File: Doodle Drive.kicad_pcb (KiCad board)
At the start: 2 copper layers, 62.9 x 80 mm, 101 parts, among them J1 USB_B, J12 PINHD_1x4_Male, J15 PINHD_1x4_Male, J2 PINHD_1x4_Male, J3 Screw_Terminal_01x02, J6 PINHD_1x2_Male, J8 PINHD_1x4_Male, J9 PINHD_1x4_Male, SW1 Push_Button, SW2 Push_Button, SW3 Push_Button, U1 STM32F411RETx, U2 DRV8825PWP, U3 DRV8825PWP, U4 DRV8825PWP, U5 DRV8825PWP, U6 AP7343-30W5-7, U7 CP2102-GMR_NRND, Y1 32.768KHz ±20ppm 12.5pF, Y2 25MHZ 9PF

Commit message: deTommaso approved version
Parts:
- removed RV5: R_Potentiometer, poti:3386P1473LF
- removed TP1, TP2, TP42, TP5: TestPoint, TestPoint:TestPoint_Pad_D1.5mm
- added RV4: R_Potentiometer, poti:3386P1473LF, F.Cu at (84.8, 73.1)
- C18, C22, C27, C32: value Bulk Capacitance. 4.7uF? -> 10uF; footprint Capacitor_SMD:C_0805_2012Metric -> Capacitor_THT:C_Radial_D5.0mm_H5.0mm_P2.00mm
- moved C11 205.5 mm to (137.2, 111.8), turned to -90 degrees
- moved C5 205.3 mm to (135.9, 114.3), turned to 180 degrees
- moved R14 202.7 mm to (135.3, 111.1), turned to 90 degrees
- moved R12 202.0 mm to (136.0, 108.0), turned to 0 degrees
- moved R13 201.1 mm to (136.0, 106.0), turned to 180 degrees
- moved R5 200.1 mm to (136.0, 104.1), turned to 0 degrees
- moved J8 199.6 mm to (131.4, 114.3), turned to -90 degrees
- moved C20 197.7 mm to (136.3, 97.8), turned to 0 degrees
- moved C21 196.7 mm to (136.3, 95.2), turned to 0 degrees
- moved U2 192.1 mm to (128.8, 107.1), turned to 180 degrees
- moved RV1 189.6 mm to (130.9, 95.9), turned to 0 degrees
- moved C18 186.8 mm to (137.2, 86.4), turned to 180 degrees
- moved R18 186.4 mm to (122.7, 111.1), turned to 0 degrees
- moved R19 183.3 mm to (123.0, 104.8), turned to 0 degrees
- moved C16 180.3 mm to (117.6, 111.8), turned to -90 degrees
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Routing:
- net GND: track 407.9 -> 518.0 mm, vias 8 -> 14
- net +3V3: track 221.9 -> 241.3 mm
- net +15V: track 304.9 -> 320.9 mm
- net Net-(U2-AVREF): track 20.7 -> 14.3 mm
- net Net-(U5-AVREF): track 21.0 -> 14.6 mm
- net Net-(U3-AVREF): track 21.5 -> 15.1 mm
- net Net-(U4-AVREF): track 20.7 -> 14.4 mm
- net PA14: track 20.7 -> 25.5 mm
- net PA13: track 9.06 -> 13.4 mm
- net PB13: track 40.1 -> 43.0 mm
- net PB6: track 30.3 -> 28.2 mm
- net PB14: track 32.2 -> 34.2 mm
- net PB15: track 29.9 -> 31.6 mm
- net +5V: track 65.5 -> 67.1 mm
- net PB12: track 43.4 -> 44.8 mm
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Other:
- board size 62.9 x 80 mm -> 80 x 62.9 mm

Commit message: bestellte version
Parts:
- C10, C7: footprint Capacitor_SMD:C_0805_2012Metric -> Capacitor_SMD:C_0402_1005Metric
- C11, C16, C26, C31: value 100nF 16V ceramic -> 100nF
- C15, C25, C30, C5: value 10nF 50V -> 10nF
- C20, C21, C23, C24, C28, C29, C33, C34: value 100nF 50V -> 100nF
- C6, C9: value 12pF -> 18pF
- L1: value 10uH ±10% -> 10uH
- R12, R13, R15, R16, R24, R25, R33, R34: footprint Resistor_SMD:R_0805_2012Metric -> Resistor_SMD:R_1206_3216Metric
- R4: value 0 -> 0ohm
- U6: value AP7343-30W5-7 -> AP7343-33W5-7
- U7: value CP2102-GMR_NRND -> CP2102-GMR
- Y2: value 25MHZ 9PF -> 25MHZ 12PF
- moved R39 77.9 mm to (136.8, 130.9), turned to 90 degrees
- moved R40 73.8 mm to (130.5, 130.9), turned to 90 degrees
- moved D6 73.8 mm to (127.3, 132.2), turned to 0 degrees
- moved J15 69.3 mm to (140.0, 121.6), turned to 0 degrees
- moved U5 67.5 mm to (132.7, 124.8), turned to -90 degrees
- moved C30 65.0 mm to (140.6, 117.0), turned to -90 degrees
- moved J3 62.4 mm to (104.2, 126.9), turned to 0 degrees
- moved R35 62.2 mm to (136.8, 117.6), turned to 180 degrees
- moved C31 60.7 mm to (137.5, 115.7), turned to 0 degrees
- moved R33 59.3 mm to (133.5, 117.0), turned to 90 degrees
- moved RV3 58.5 mm to (121.6, 122.7), turned to 90 degrees
- moved J1 57.8 mm to (95.4, 121.5), turned to 180 degrees
- moved C5 57.7 mm to (140.6, 56.8), turned to -90 degrees
- moved R34 57.1 mm to (131.0, 117.0), turned to -90 degrees
- moved C11 56.3 mm to (138.1, 55.5), turned to 0 degrees
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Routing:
- net GND: track 518.0 -> 541.4 mm, vias 14 -> 15
- net +3V3: track 241.3 -> 235.8 mm
- net +15V: track 320.9 -> 325.6 mm
- net PC14: track 10.9 -> 8.61 mm
- net PC15: track 8.78 -> 7.83 mm
- net Net-(U3-AVREF): track 15.1 -> 14.9 mm, vias 2 -> 1
- net Net-(U5-AVREF): track 14.6 -> 14.8 mm, vias 2 -> 1
- net Net-(U4-AVREF): vias 2 -> 1
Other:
- board size 80 x 62.9 mm -> 62.9 x 80 mm
- board text added: "5BEL 12/2023"
- board text added: "Doodle Drive V1.0"
- board text added: "ELIA VANDINI"

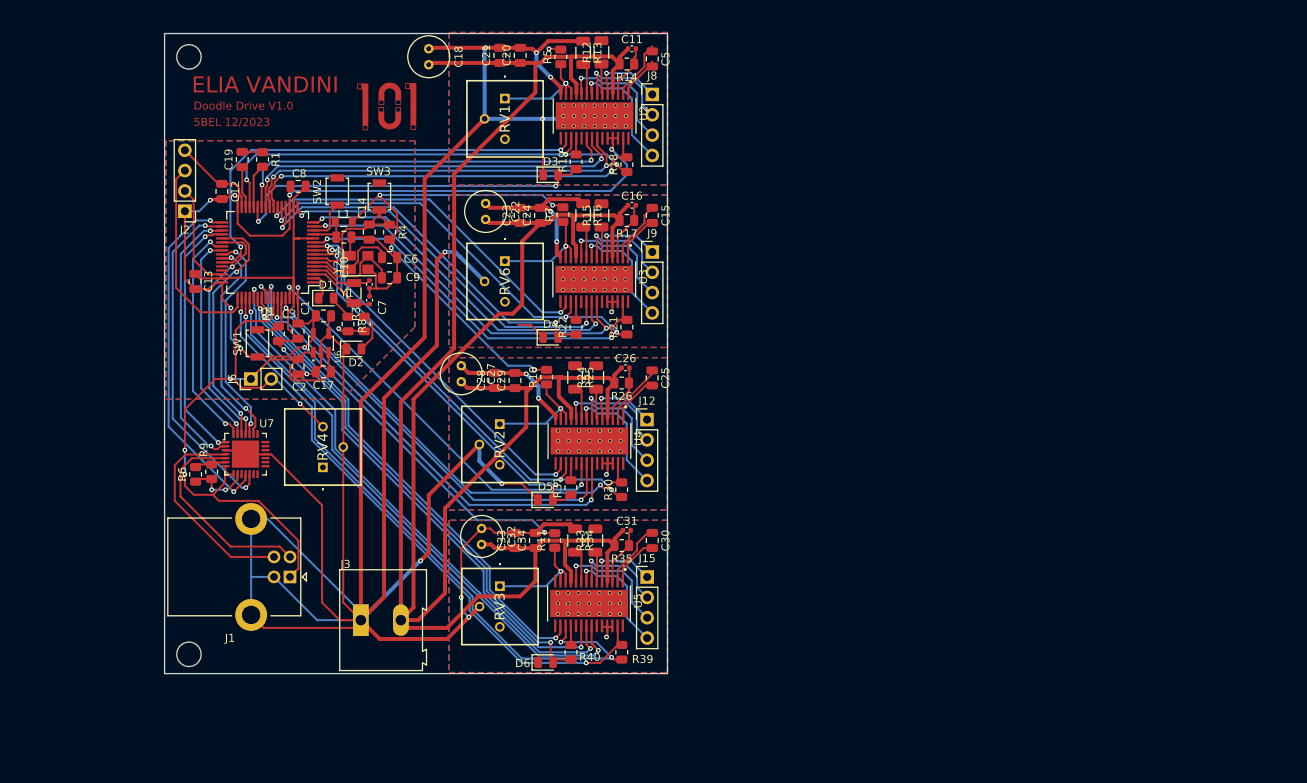
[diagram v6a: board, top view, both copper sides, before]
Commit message: reworked single motor drive module
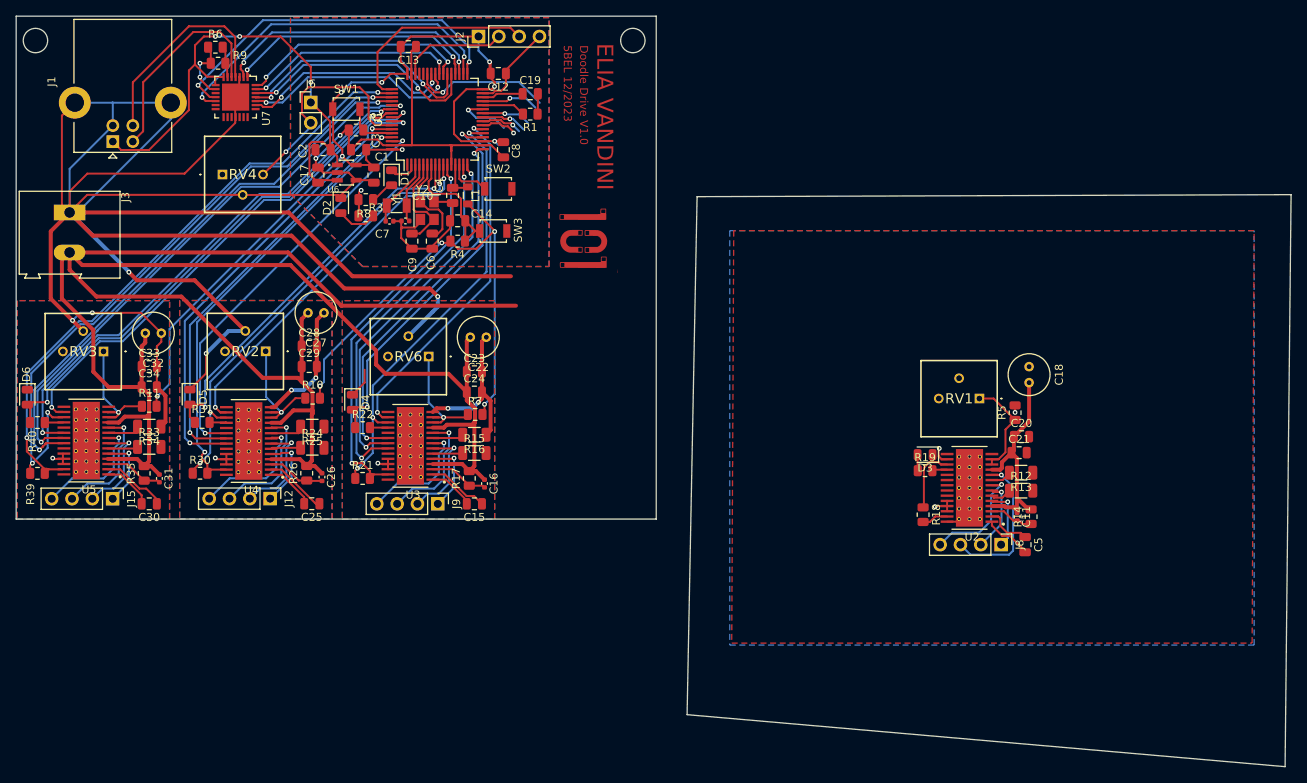
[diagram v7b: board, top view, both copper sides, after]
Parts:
- moved C18 84.9 mm to (187.8, 95.2)
- moved C21 81.7 mm to (186.5, 106.0), turned to 0 degrees
- moved C20 78.7 mm to (186.8, 104.0), turned to 0 degrees
- moved C5 76.5 mm to (187.2, 117.5)
- moved R39 76.4 mm to (63.8, 108.6), turned to 0 degrees
- moved R14 75.9 mm to (188.0, 114.0), turned to 90 degrees
- moved R12 75.9 mm to (186.8, 110.8), turned to 0 degrees
- moved R13 75.8 mm to (186.8, 108.5), turned to 180 degrees
- moved C11 75.8 mm to (186.2, 114.0), turned to -90 degrees
- moved D6 72.8 mm to (62.5, 99.1), turned to -90 degrees
- moved R40 72.6 mm to (63.8, 102.2), turned to 0 degrees
- moved R5 72.1 mm to (186.0, 101.0)
- moved J8 71.2 mm to (184.2, 117.5), turned to -90 degrees
- moved RV1 70.2 mm to (181.5, 99.2), turned to 0 degrees
- moved J15 67.5 mm to (73.2, 111.8), turned to -90 degrees
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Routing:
- net GND: track 541.4 -> 479.9 mm, vias 15 -> 11
- net +3V3: track 235.8 -> 188.8 mm
- net PC4: track 50.2 -> 5.16 mm, vias 2 -> 1
- net PA7: track 51.8 -> 7.81 mm, vias 2 -> 1
- net PC5: track 49.6 -> 5.73 mm, vias 2 -> 1
- net DIR2: track 49.2 -> 6.20 mm, vias 2 -> 1
- net PB10: track 56.8 -> 15.5 mm, vias 3 -> 1
- net PA10: track 57.8 -> 19.6 mm
- net PB1: track 46.3 -> 9.23 mm, vias 2 -> 1
- net +15V: track 325.6 -> 298.9 mm
- net Net-(U2-AOUT2): track 12.9 -> 8.93 mm
- net Net-(U2-BOUT1): track 15.7 -> 18.6 mm
- net Net-(U2-AOUT1): track 9.43 -> 7.73 mm
- net Net-(U2-CP2): track 7.41 -> 5.76 mm
- net Net-(U2-BOUT2): track 15.3 -> 13.9 mm
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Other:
- board size 62.9 x 80 mm -> 159.4 x 93.8 mm

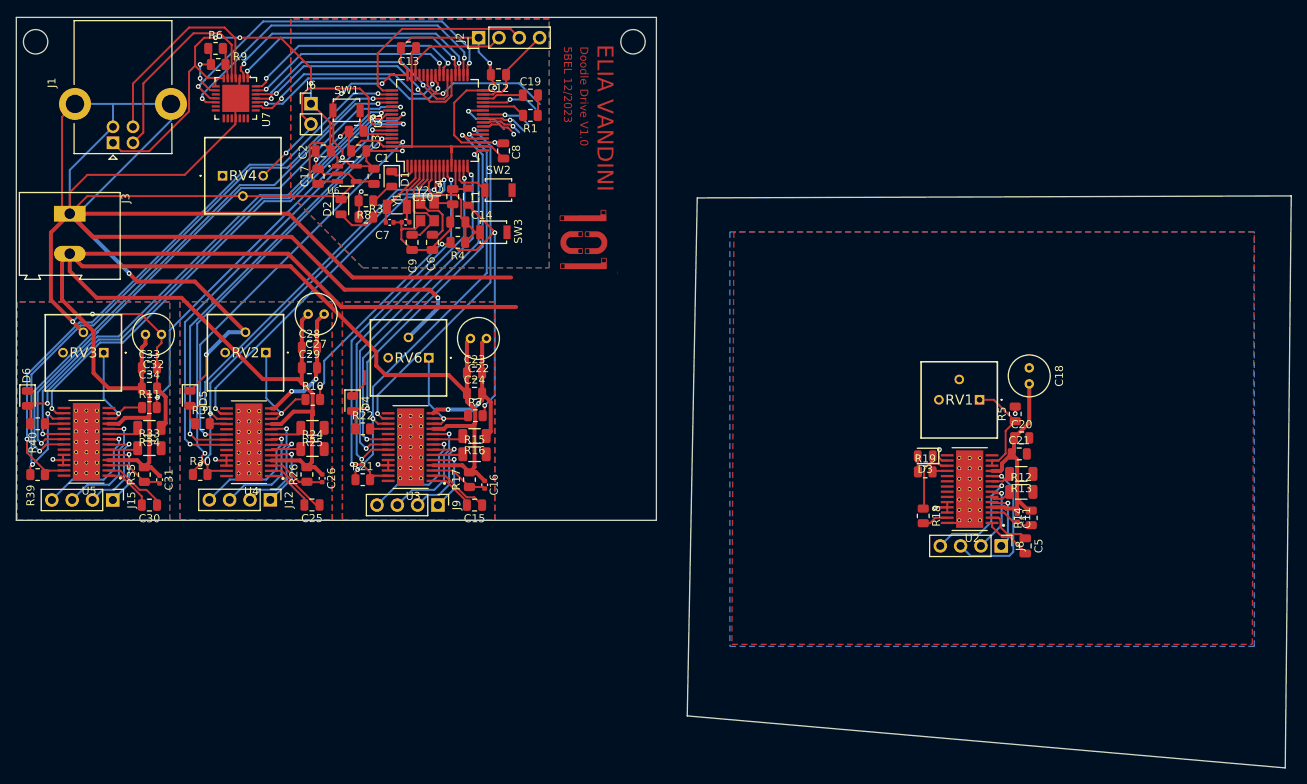
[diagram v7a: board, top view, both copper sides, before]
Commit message: restiched everything and removed polygons
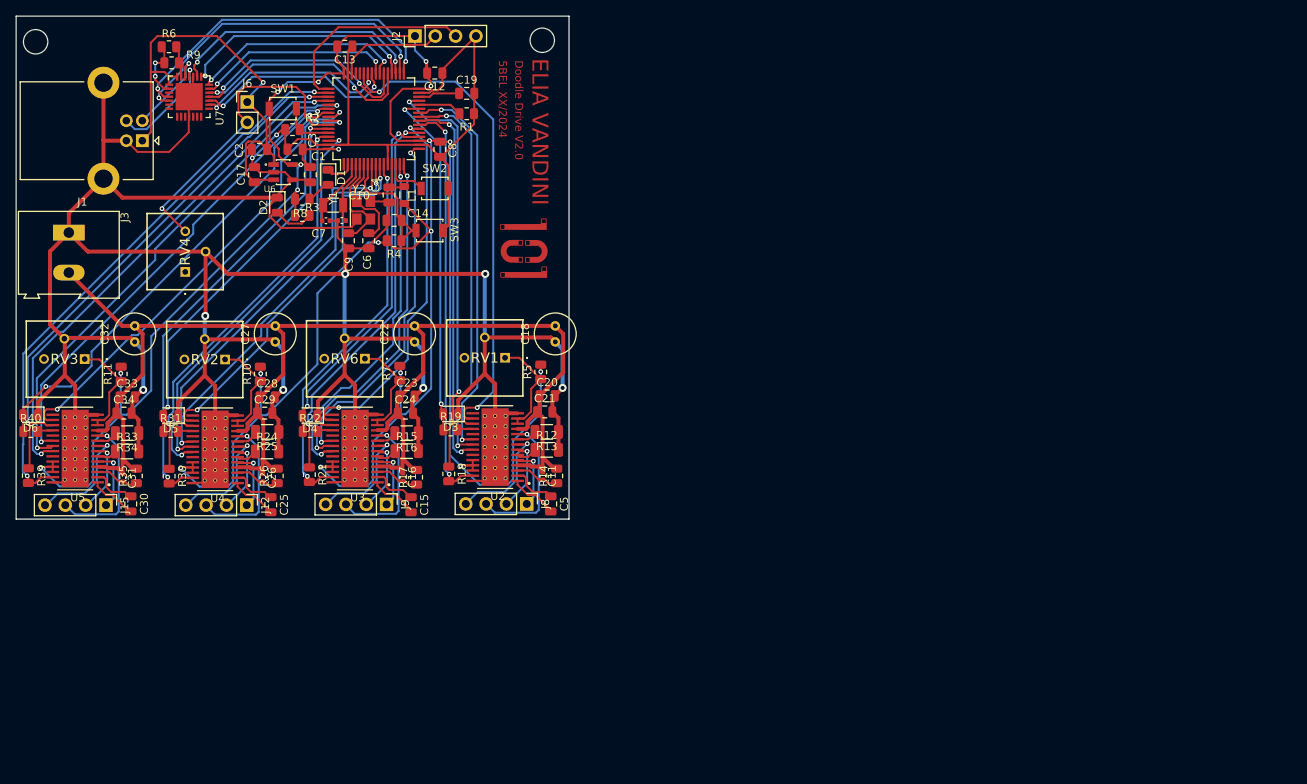
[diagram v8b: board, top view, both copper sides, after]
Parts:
- moved C20 59.5 mm to (127.5, 98.8)
- moved U2 59.5 mm to (121.0, 105.2)
- moved C11 59.5 mm to (126.9, 108.8)
- moved C21 59.5 mm to (127.2, 100.8)
- moved C5 59.5 mm to (127.9, 112.2)
- moved D3 59.5 mm to (115.4, 101.0)
- moved J8 59.5 mm to (124.9, 112.2)
- moved R12 59.5 mm to (127.4, 105.5)
- moved R13 59.5 mm to (127.4, 103.2)
- moved R14 59.5 mm to (128.7, 108.8)
- moved R18 59.5 mm to (115.2, 108.5)
- moved R19 59.5 mm to (115.4, 103.0)
- moved R5 59.5 mm to (126.7, 95.8)
- moved RV1 59.5 mm to (122.2, 94.0)
- moved C18 59.3 mm to (128.5, 92.0), turned to 90 degrees
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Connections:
- D5 pad 2: PC0 -> PB7
- R30 pad 1: PC1 -> PB8
- R30 pad 2: PB8 -> PB5
- R31 pad 1: PC0 -> PB7
- U1 pad 62: DIR3 -> PB9
- U1 pad 9: PC1 -> DIR3
- U4 pad 17: PC1 -> PB8
- U4 pad 21: PB7 -> PC0
- U4 pad 22: PB5 -> PB9
- U4 pad 27: PB8 -> PB5
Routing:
- net +3V3: track 188.8 -> 339.7 mm, vias 18 -> 19
- net +15V: track 298.9 -> 184.5 mm
- net PC1: track 56.4 -> 0.00 mm, vias 3 -> 0
- net PB9: track 0.00 -> 51.8 mm, vias 0 -> 2
- net PC5: track 5.73 -> 49.1 mm, vias 1 -> 2
- net PA7: track 7.81 -> 51.0 mm, vias 1 -> 2
- net DIR2: track 6.20 -> 48.9 mm, vias 1 -> 2
- net PC4: track 5.16 -> 47.6 mm, vias 1 -> 2
- net PA10: track 19.6 -> 60.9 mm
- net PB10: track 15.5 -> 54.5 mm, vias 1 -> 2
- net PB1: track 9.23 -> 43.9 mm, vias 1 -> 2
- net GND: track 479.9 -> 506.6 mm, vias 11 -> 9
- net Net-(J1-D-): track 26.4 -> 11.4 mm, vias 0 -> 1
- net Net-(J1-D+): track 26.6 -> 13.5 mm, vias 0 -> 1
- net PC10: track 81.3 -> 68.3 mm, vias 3 -> 2
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- removed copper zone on B.Cu, net +3V3
- removed copper zone on F.Cu, net GND
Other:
- board size 159.4 x 93.8 mm -> 69.1 x 62.9 mm
- board text added: "5BEL XX/2024"
- board text added: "Doodle Drive V2.0"
- board text removed: "5BEL 12/2023"
- board text removed: "Doodle Drive V1.0"
